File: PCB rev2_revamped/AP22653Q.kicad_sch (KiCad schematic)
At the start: 6 parts, among them U4 AP22815AWT-7

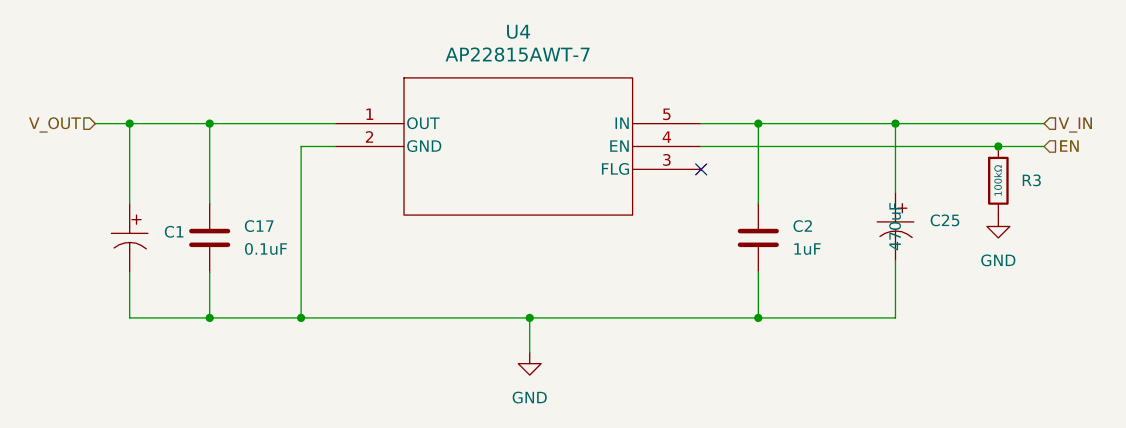
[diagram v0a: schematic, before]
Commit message: Add CAN-enabled PCB design
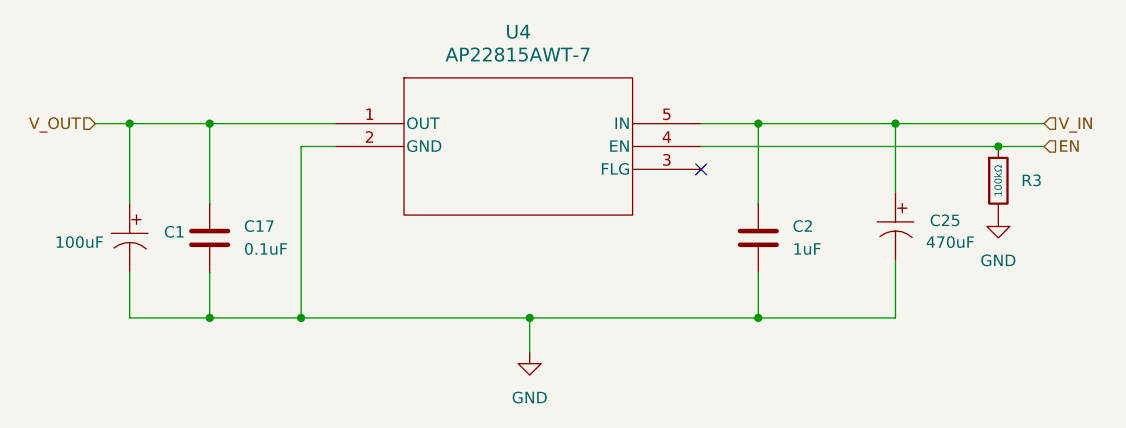
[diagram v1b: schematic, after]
